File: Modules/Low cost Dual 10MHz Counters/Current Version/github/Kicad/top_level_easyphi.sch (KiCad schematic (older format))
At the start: 126 parts, among them P2 CONN_20X2, U11 RLP1-600-800, U13 SN74LVC1T45, U14 SN74LVC1G175, U17 RLP1-600-800, U18 RLP1-600-800, U19 RLP1-600-800, U20 RLP1-600-800, U21 RLP1-600-800, U22 CONNEC_QMA_ANO_2622-4035, U24 CONNEC_SMA_132203, U25 CONNEC_QMA_ANO_2622-4035, U26 CONNEC_SMA_132203, U27 CONNEC_SMA_132203, U28 CONNEC_QMA_ANO_2622-4035, U29 SY89840U, U30 NB4L52, U31 NB4L52, U32 MAX9203EKA-T, U33 SN74LVC1T45, U34 SN74LVC1T45, U35 TPS7A4901, U36 MAX9203EKA-T

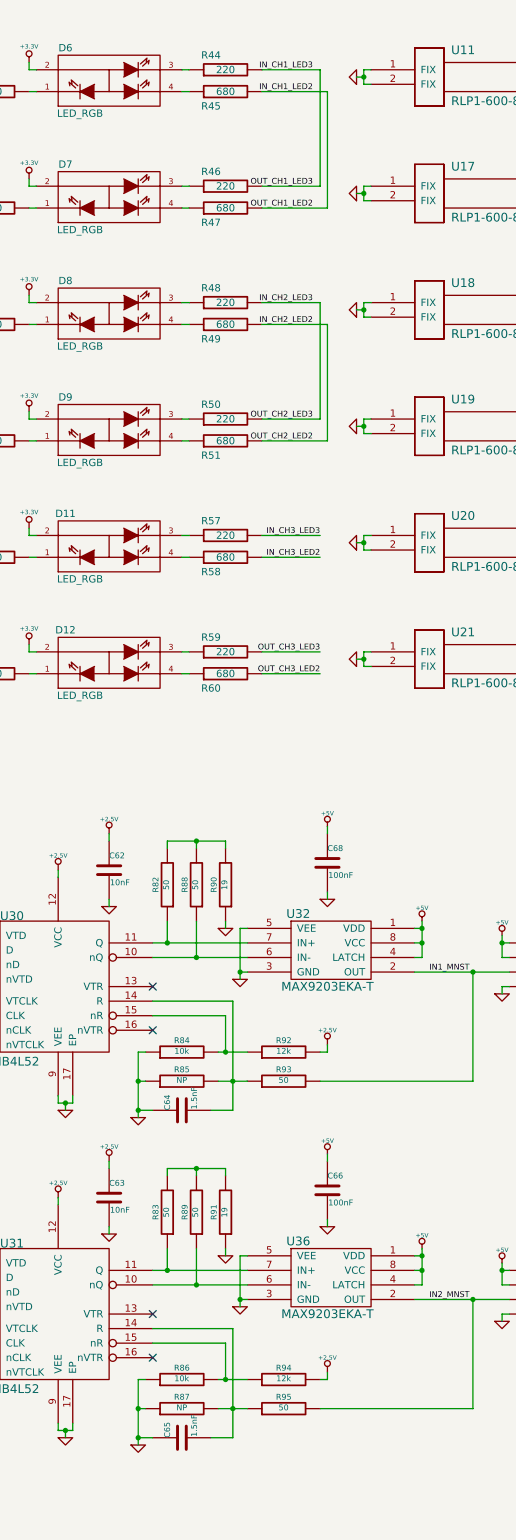
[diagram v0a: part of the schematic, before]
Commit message: update counters
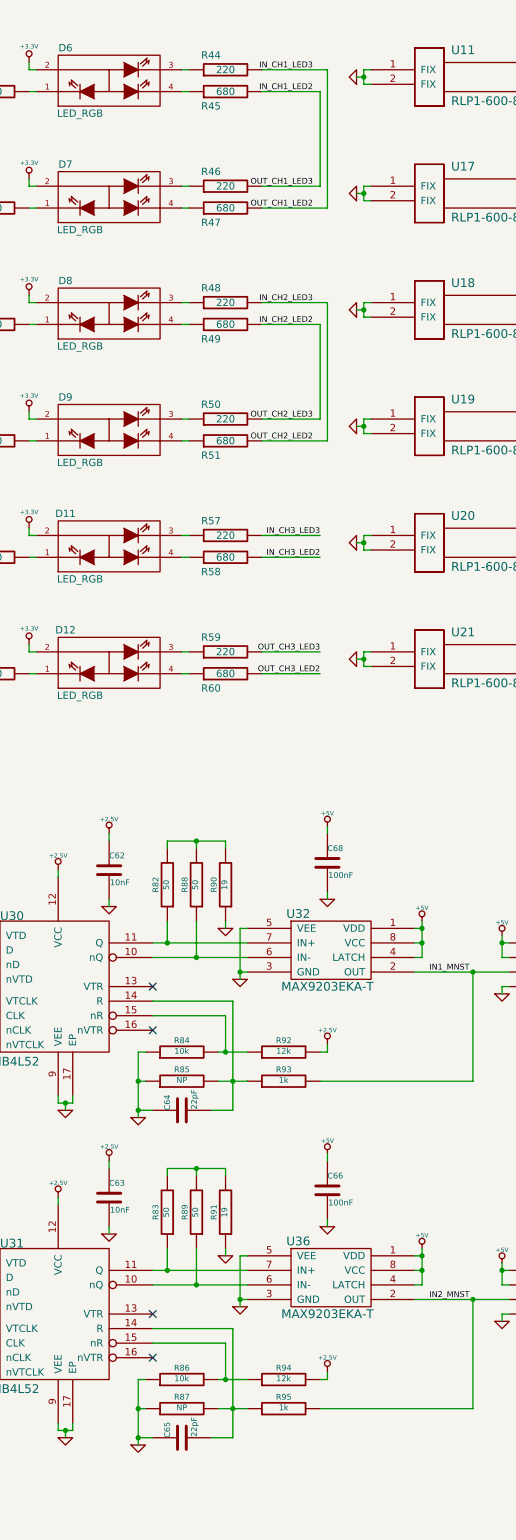
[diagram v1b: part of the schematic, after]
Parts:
- C64, C65: value 1.5nF -> 22pF
- R93, R95: value 50 -> 1k
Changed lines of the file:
@@
 Sheet 1 2
 Title "Low cost dual 10MHz Counters"
-Date "2 jan 2014"
+Date "12 mar 2014"
 Rev "1.0"
 Comp "University of Geneva                       www.easy.phi.ch"
@@
 	14050 850  14350 850
 Wire Wire Line
-	11850 1000 12250 1000
+	11850 1000 12300 1000
 Connection ~ 14050 1050
 Wire Wire Line
@@
 	9300 1150 9750 1150
 Wire Wire Line
-	11850 1150 12300 1150
+	11850 1150 12250 1150
 Wire Wire Line
 	11850 1950 12300 1950
@@
 	11850 1800 12250 1800
 Wire Wire Line
-	11850 2600 12250 2600
+	11850 2600 12300 2600
 Wire Wire Line
 	11300 2600 11350 2600
@@
 	9300 2750 9750 2750
 Wire Wire Line
-	11850 2750 12300 2750
+	11850 2750 12250 2750
 Wire Wire Line
 	11850 3550 12300 3550
@@
 P 12000 7950
 F 0 "R93" V 12080 7950 40  0000 C CNN
-F 1 "50" V 12007 7951 40  0000 C CNN
+F 1 "1k" V 12007 7951 40  0000 C CNN
 F 2 "~" V 11930 7950 30  0000 C CNN
 F 3 "~" H 12000 7950 30  0000 C CNN
@@
 P 11300 8150
 F 0 "C64" H 11300 8250 40  0000 L CNN
-F 1 "1.5nF" H 11306 8065 40  0000 L CNN
+F 1 "22pF" H 11306 8065 40  0000 L CNN
 F 2 "~" H 11338 8000 30  0000 C CNN
 F 3 "~" H 11300 8150 60  0000 C CNN
@@
 P 12000 10200
 F 0 "R95" V 12080 10200 40  0000 C CNN
-F 1 "50" V 12007 10201 40  0000 C CNN
+F 1 "1k" V 12007 10201 40  0000 C CNN
 F 2 "~" V 11930 10200 30  0000 C CNN
 F 3 "~" H 12000 10200 30  0000 C CNN
@@
 P 11300 10400
 F 0 "C65" H 11300 10500 40  0000 L CNN
-F 1 "1.5nF" H 11306 10315 40  0000 L CNN
+F 1 "22pF" H 11306 10315 40  0000 L CNN
 F 2 "~" H 11338 10250 30  0000 C CNN
 F 3 "~" H 11300 10400 60  0000 C CNN
@@
 Wire Wire Line
 	9300 2750 9300 3550
-Wire Wire Line
-	12250 3400 12250 2600
-Wire Wire Line
-	12300 3550 12300 2750
 Text Label 3650 7650 2    40   ~ 0
 IN_CH2_LED3
@@
 Wire Wire Line
 	9300 1150 9300 1950
-Wire Wire Line
-	12250 1800 12250 1000
-Wire Wire Line
-	12300 1950 12300 1150
 Text Label 3650 6250 2    40   ~ 0
 IN_CH1_LED3
@@
 	1    0    0    -1
 $EndComp
+Wire Wire Line
+	12250 1800 12250 1150
+Wire Wire Line
+	12300 1950 12300 1000
+Wire Wire Line
+	12250 3400 12250 2750
+Wire Wire Line
+	12300 3550 12300 2600
 $EndSCHEMATC

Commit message: update specs
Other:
- note added: "12ns pulse"
- note removed: "200ns pulse"
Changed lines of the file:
@@
 Sheet 1 2
 Title "Low cost dual 10MHz Counters"
-Date "12 mar 2014"
+Date "17 apr 2014"
 Rev "1.0"
 Comp "University of Geneva                       www.easy.phi.ch"
@@
 $EndComp
 Text Notes 15500 9350 0    40   ~ 0
-200ns pulse
+12ns pulse
 Text Notes 15550 7100 0    40   ~ 0
-200ns pulse
+12ns pulse
 Connection ~ 6200 3200
 Text Label 6100 3200 0    40   ~ 0
